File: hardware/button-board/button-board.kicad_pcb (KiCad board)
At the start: 2 copper layers, 37.3 x 38.2 mm, 10 parts, among them J1 Big button, J2 BUTTON, J3 BUTTON

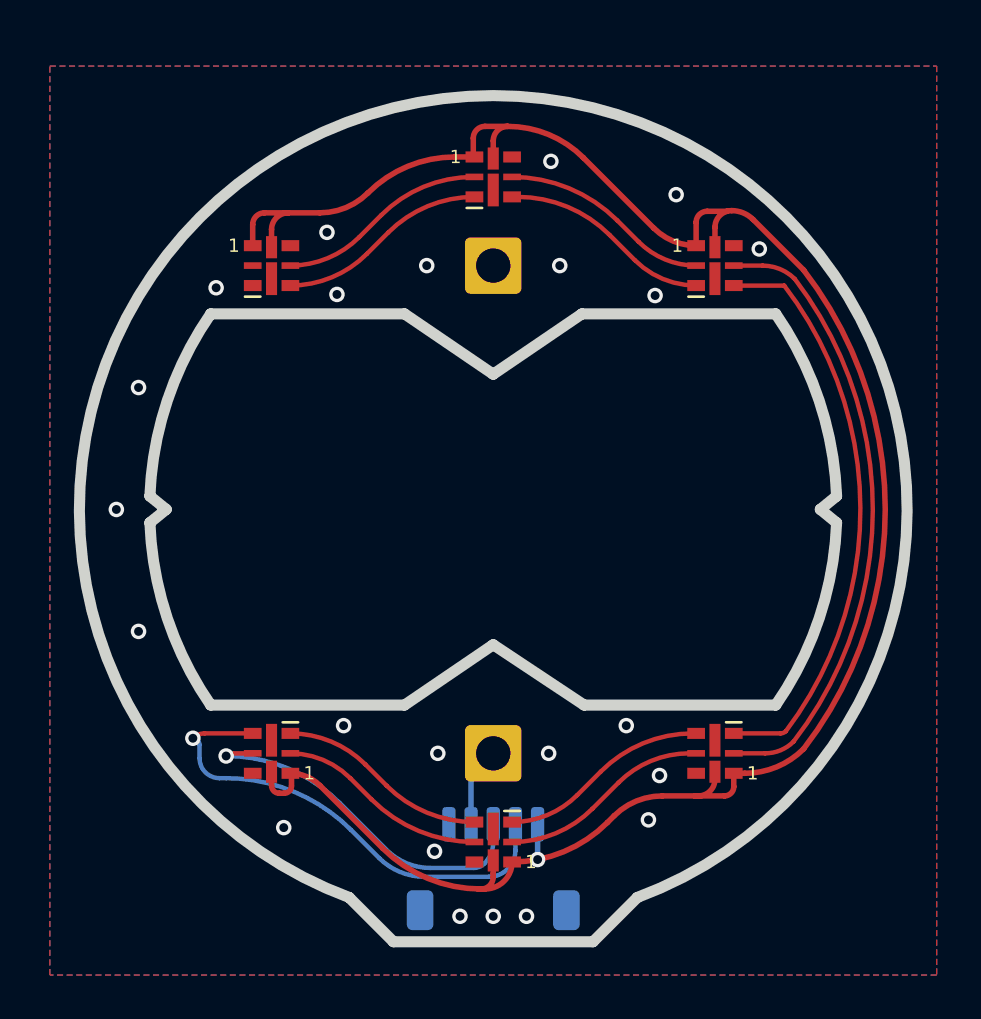
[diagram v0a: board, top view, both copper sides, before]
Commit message: hardware: Revise button board- move all components to front side, update footprint for LEDs, add caps, change friction tabs to avoid interference with switch locking tabs
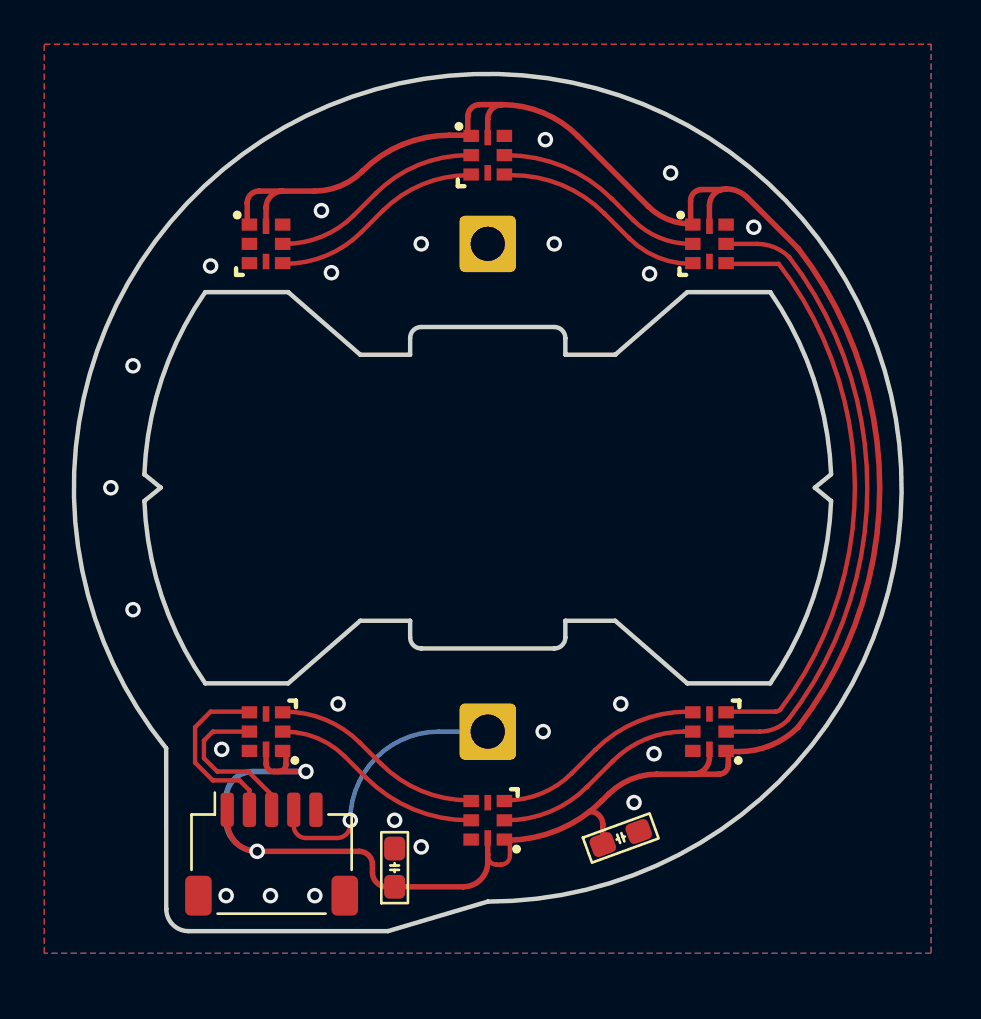
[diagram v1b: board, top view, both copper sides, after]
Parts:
- added C1: 10u, winterbloom:C_0603_HandSolder, F.Cu at (51.8, 97.1)
- added C2: 100n, winterbloom:C_0603_HandSolder, F.Cu at (62.0, 95.8)
- D1, D2, D3, D4, D5, D6: footprint LED_SMD:LED-APA102-2020 -> winterbloom:LED-APA102-2020
- J1: moved to F.Cu
- moved REF** 17.0 mm to (46.2, 94.9)
- moved J1 10.0 mm to (46.2, 96.5), turned to 0 degrees
- moved D2 1.01 mm to (66.0, 91.0)
- moved D3 1.01 mm to (66.0, 69.0)
- moved D1 1.01 mm to (56.0, 95.0)
- moved D4 1.01 mm to (56.0, 65.0)
- moved D5 1.01 mm to (46.0, 69.0)
- moved D6 1.01 mm to (46.0, 91.0)
- moved J2 1.01 mm to (56.0, 91.0)
- moved J3 1.01 mm to (56.0, 69.0)
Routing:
- net /BUTTON_DOTSTAR_DATA: track 21.7 -> 8.08 mm, vias 1 -> 0
- net +3V3: track 95.0 -> 108.5 mm, vias 1 -> 2
- net /BIG_BUTTON: track 2.20 -> 12.4 mm, vias 0 -> 1
- net /BUTTON_DOTSTAR_CLK: track 16.4 -> 7.32 mm, vias 1 -> 0
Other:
- board size 37.3 x 38.2 mm -> 37.3 x 38.7 mm
- board text added: "PCB Specifications: - 2 copper layers - Size: 37.4 x 38.7 mm - Thickness: 1.6 mm - Material: FR4 TG-140+ - Min track width/spacing: 0.153 mm (6 mil) - Min hole size: 0.3 mm - Soldermask: Pink/Purple/Matte Black - Silkscreen: Black/White - Finish: ENIG 2U{dblquote} - Copper: 1 oz - UL Marking: None"
- board text removed: "PCB Specifications: - 2 copper layers - Size: 37.4 x 38.2 mm - Thickness: 1.6 mm - Material: FR4 TG-140+ - Min track width/spacing: 0.153 mm (6 mil) - Min hole size: 0.3 mm - Soldermask: Pink/Purple/Matte Black - Silkscreen: Black/White - Finish: ENIG 2U{dblquote} - Copper: 1 oz - UL Marking: None"
